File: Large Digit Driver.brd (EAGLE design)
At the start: 45.7 x 22.9 mm, 26 parts, among them U1 TPIC6C596

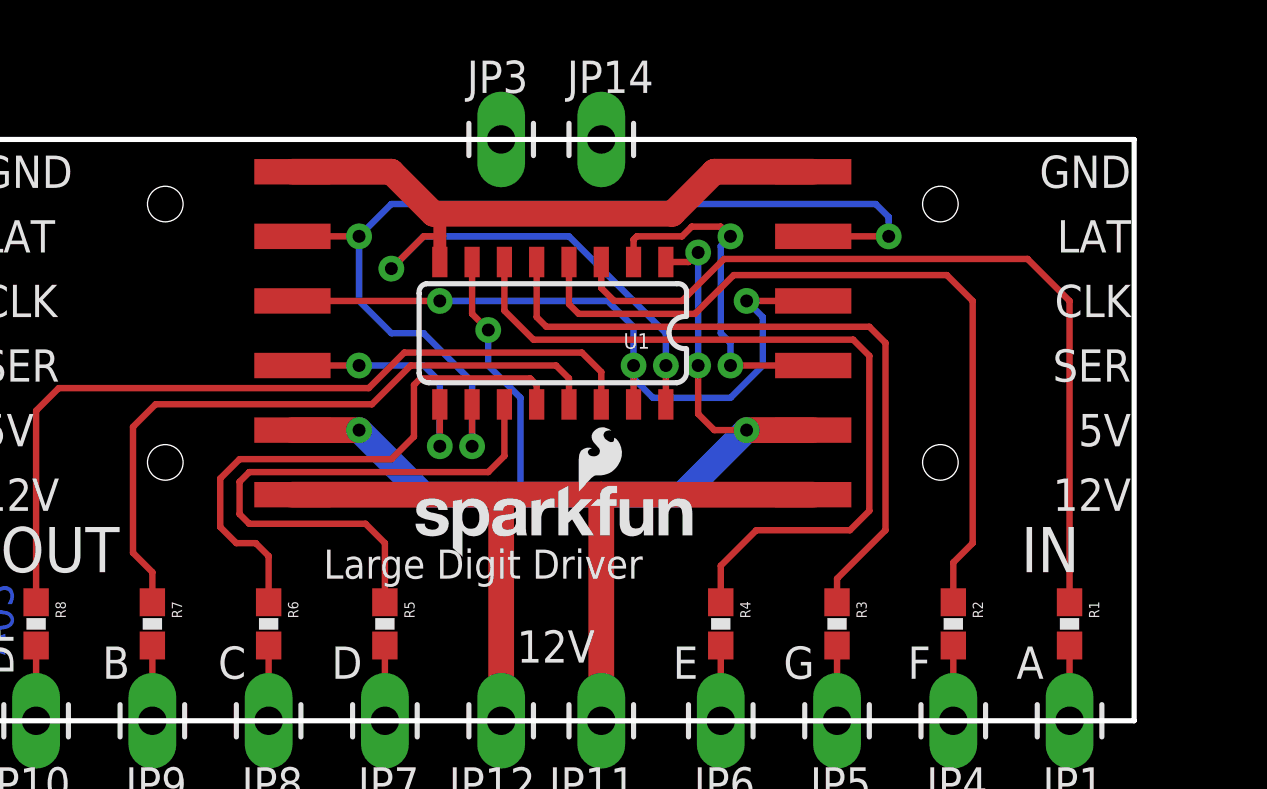
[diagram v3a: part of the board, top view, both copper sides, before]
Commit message: Added fiducials for issue #1.
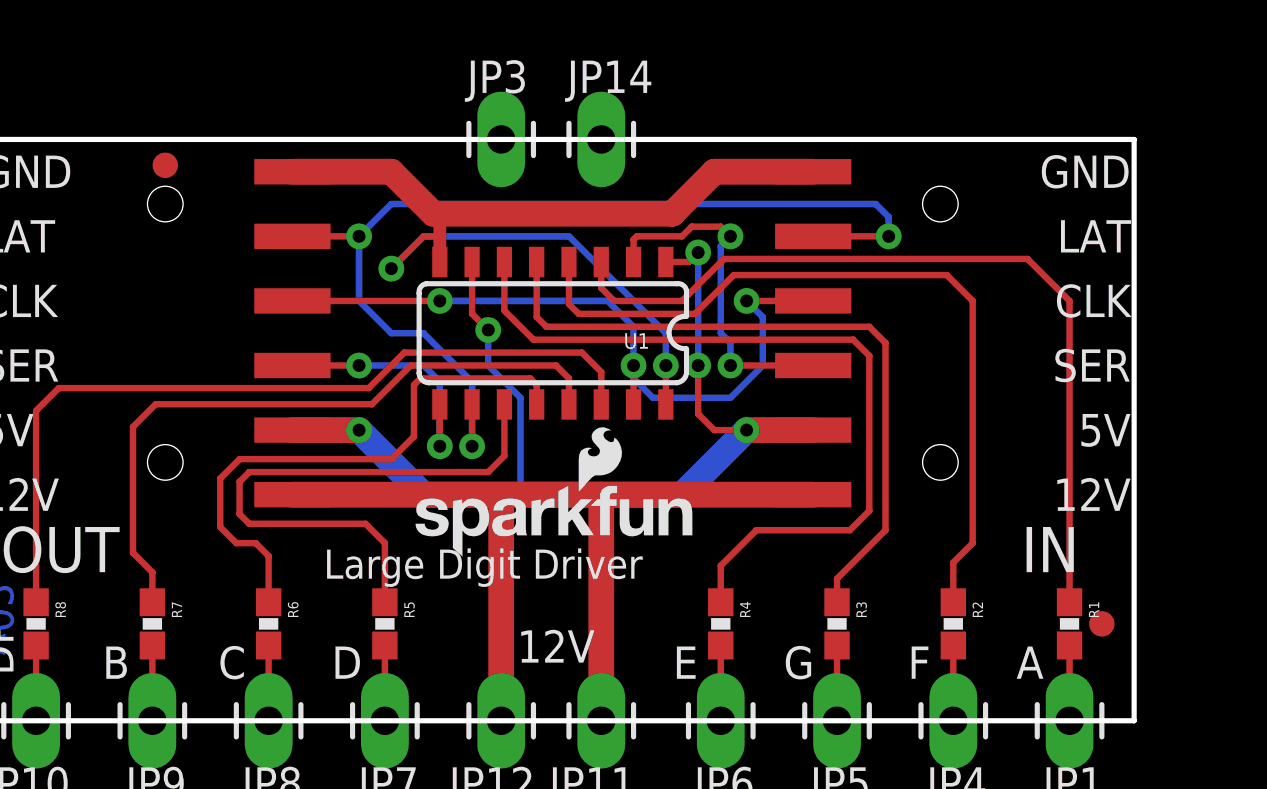
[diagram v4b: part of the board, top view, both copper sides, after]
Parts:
- added FID1, FID2: FIDUCIAL1X2, SparkFun-Aesthetics:FIDUCIAL-1X2

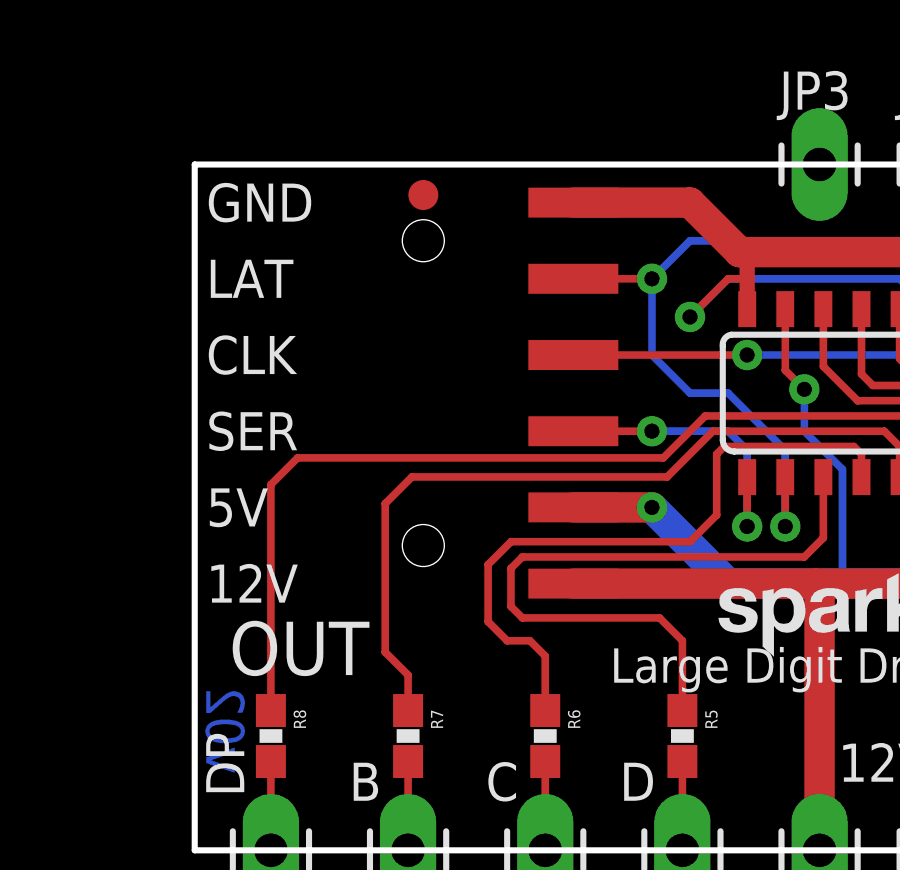
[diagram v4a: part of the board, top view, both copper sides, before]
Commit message: moved fiducial from under header
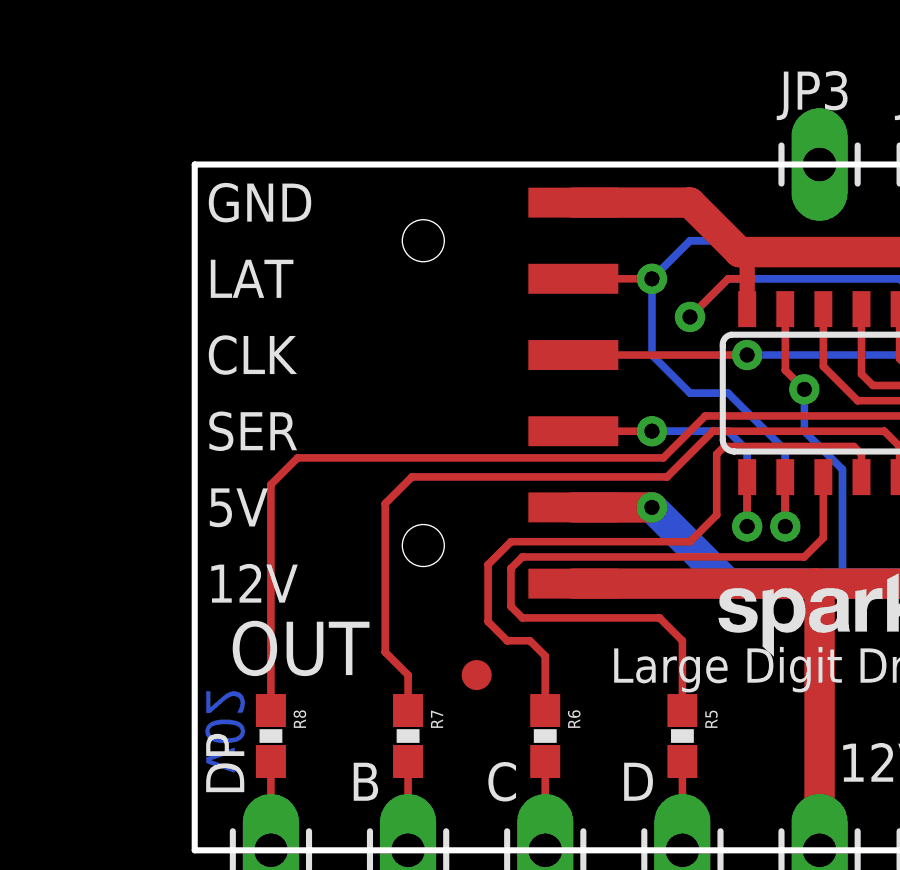
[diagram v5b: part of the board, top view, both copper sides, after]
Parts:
- moved FID1 16.1 mm to (9.40, 5.84)
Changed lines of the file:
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@@
 <?xml version="1.0" encoding="utf-8"?>
 <!DOCTYPE eagle SYSTEM "eagle.dtd">
-<eagle version="7.2.0">
+<eagle version="6.6.0">
 <drawing>
 <settings>
@@
 <setting verticaltext="up"/>
 </settings>
-<grid distance="0.05" unitdist="inch" unit="inch" style="lines" multiple="1" display="yes" altdistance="0.005" altunitdist="inch" altunit="inch"/>
+<grid distance="0.01" unitdist="inch" unit="inch" style="lines" multiple="1" display="yes" altdistance="0.001" altunitdist="inch" altunit="inch"/>
 <layers>
 <layer number="1" name="Top" color="4" fill="1" visible="yes" active="yes"/>
@@
 <layer number="18" name="Vias" color="2" fill="1" visible="yes" active="yes"/>
 <layer number="19" name="Unrouted" color="6" fill="1" visible="yes" active="yes"/>
-<layer number="20" name="Dimension" color="15" fill="1" visible="yes" active="yes"/>
-<layer number="21" name="tPlace" color="16" fill="1" visible="yes" active="yes"/>
-<layer number="22" name="bPlace" color="14" fill="1" visible="yes" active="yes"/>
+<layer number="20" name="Dimension" color="6" fill="1" visible="yes" active="yes"/>
+<layer number="21" name="tPlace" color="6" fill="1" visible="yes" active="yes"/>
+<layer number="22" name="bPlace" color="6" fill="1" visible="yes" active="yes"/>
 <layer number="23" name="tOrigins" color="15" fill="1" visible="yes" active="yes"/>
 <layer number="24" name="bOrigins" color="15" fill="1" visible="yes" active="yes"/>
-<layer number="25" name="tNames" color="7" fill="1" visible="no" active="yes"/>
-<layer number="26" name="bNames" color="7" fill="1" visible="no" active="yes"/>
-<layer number="27" name="tValues" color="7" fill="1" visible="no" active="yes"/>
-<layer number="28" name="bValues" color="7" fill="1" visible="no" active="yes"/>
-<layer number="29" name="tStop" color="5" fill="1" visible="no" active="yes"/>
-<layer number="30" name="bStop" color="7" fill="6" visible="no" active="yes"/>
-<layer number="31" name="tCream" color="7" fill="4" visible="no" active="yes"/>
-<layer number="32" name="bCream" color="7" fill="5" visible="no" active="yes"/>
+<layer number="25" name="tNames" color="7" fill="1" visible="yes" active="yes"/>
+<layer number="26" name="bNames" color="7" fill="1" visible="yes" active="yes"/>
+<layer number="27" name="tValues" color="7" fill="1" visible="yes" active="yes"/>
+<layer number="28" name="bValues" color="7" fill="1" visible="yes" active="yes"/>
+<layer number="29" name="tStop" color="5" fill="1" visible="yes" active="yes"/>
+<layer number="30" name="bStop" color="7" fill="6" visible="yes" active="yes"/>
+<layer number="31" name="tCream" color="7" fill="4" visible="yes" active="yes"/>
+<layer number="32" name="bCream" color="7" fill="5" visible="yes" active="yes"/>
 <layer number="33" name="tFinish" color="6" fill="3" visible="yes" active="yes"/>
 <layer number="34" name="bFinish" color="6" fill="6" visible="yes" active="yes"/>
-<layer number="35" name="tGlue" color="7" fill="4" visible="no" active="yes"/>
-<layer number="36" name="bGlue" color="7" fill="5" visible="no" active="yes"/>
+<layer number="35" name="tGlue" color="7" fill="4" visible="yes" active="yes"/>
+<layer number="36" name="bGlue" color="7" fill="5" visible="yes" active="yes"/>
 <layer number="37" name="tTest" color="7" fill="1" visible="yes" active="yes"/>
 <layer number="38" name="bTest" color="7" fill="1" visible="yes" active="yes"/>
-<layer number="39" name="tKeepout" color="4" fill="11" visible="no" active="yes"/>
-<layer number="40" name="bKeepout" color="1" fill="11" visible="no" active="yes"/>
-<layer number="41" name="tRestrict" color="4" fill="10" visible="no" active="yes"/>
-<layer number="42" name="bRestrict" color="1" fill="10" visible="no" active="yes"/>
-<layer number="43" name="vRestrict" color="2" fill="10" visible="no" active="yes"/>
-<layer number="44" name="Drills" color="7" fill="1" visible="no" active="yes"/>
+<layer number="39" name="tKeepout" color="4" fill="11" visible="yes" active="yes"/>
+<layer number="40" name="bKeepout" color="1" fill="11" visible="yes" active="yes"/>
+<layer number="41" name="tRestrict" color="4" fill="10" visible="yes" active="yes"/>
+<layer number="42" name="bRestrict" color="1" fill="10" visible="yes" active="yes"/>
+<layer number="43" name="vRestrict" color="2" fill="10" visible="yes" active="yes"/>
+<layer number="44" name="Drills" color="7" fill="1" visible="yes" active="yes"/>
 <layer number="45" name="Holes" color="7" fill="1" visible="yes" active="yes"/>
-<layer number="46" name="Milling" color="3" fill="1" visible="no" active="yes"/>
-<layer number="47" name="Measures" color="7" fill="1" visible="no" active="yes"/>
-<layer number="48" name="Document" color="7" fill="1" visible="no" active="yes"/>
-<layer number="49" name="Reference" color="11" fill="1" visible="no" active="yes"/>
+<layer number="46" name="Milling" color="3" fill="1" visible="yes" active="yes"/>
+<layer number="47" name="Measures" color="7" fill="1" visible="yes" active="yes"/>
+<layer number="48" name="Document" color="7" fill="1" visible="yes" active="yes"/>
+<layer number="49" name="Reference" color="11" fill="1" visible="yes" active="yes"/>
 <layer number="50" name="dxf" color="7" fill="1" visible="no" active="no"/>
 <layer number="51" name="tDocu" color="6" fill="1" visible="yes" active="yes"/>
-<layer number="52" name="bDocu" color="7" fill="1" visible="no" active="yes"/>
+<layer number="52" name="bDocu" color="7" fill="1" visible="yes" active="yes"/>
 <layer number="53" name="tGND_GNDA" color="7" fill="9" visible="no" active="no"/>
 <layer number="54" name="bGND_GNDA" color="1" fill="9" visible="no" active="no"/>
@@
 <pass name="Default">
 <param name="RoutingGrid" value="50mil"/>
-<param name="AutoGrid" value="1"/>
-<param name="Efforts" value="0"/>
-<param name="TopRouterVariant" value="1"/>
 <param name="tpViaShape" value="round"/>
 <param name="PrefDir.1" value="|"/>
@@
 <element name="JP3" library="SparkFun-Connectors" package="1X01_LONGPAD" value="Anchor" x="20.828" y="22.86"/>
 <element name="JP14" library="SparkFun-Connectors" package="1X01_LONGPAD" value="Anchor" x="24.765" y="22.86"/>
-<element name="FID1" library="SparkFun-Aesthetics" package="FIDUCIAL-1X2" value="FIDUCIAL1X2" x="7.62" y="21.844"/>
+<element name="FID1" library="SparkFun-Aesthetics" package="FIDUCIAL-1X2" value="FIDUCIAL1X2" x="9.398" y="5.842"/>
 <element name="FID2" library="SparkFun-Aesthetics" package="FIDUCIAL-1X2" value="FIDUCIAL1X2" x="44.45" y="3.81"/>
 </elements>

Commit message: moved it again, better this time
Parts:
- moved FID1 18.7 mm to (18.5, 22.1)
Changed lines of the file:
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@@
 <element name="JP3" library="SparkFun-Connectors" package="1X01_LONGPAD" value="Anchor" x="20.828" y="22.86"/>
 <element name="JP14" library="SparkFun-Connectors" package="1X01_LONGPAD" value="Anchor" x="24.765" y="22.86"/>
-<element name="FID1" library="SparkFun-Aesthetics" package="FIDUCIAL-1X2" value="FIDUCIAL1X2" x="9.398" y="5.842"/>
+<element name="FID1" library="SparkFun-Aesthetics" package="FIDUCIAL-1X2" value="FIDUCIAL1X2" x="18.542" y="22.098"/>
 <element name="FID2" library="SparkFun-Aesthetics" package="FIDUCIAL-1X2" value="FIDUCIAL1X2" x="44.45" y="3.81"/>
 </elements>
